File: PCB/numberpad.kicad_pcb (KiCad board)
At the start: 2 copper layers, 97 x 127.2 mm, 73 parts, among them J1 Light_Sensor, J2 Rotary_Encoder, J3 Screen_Connector, J4 FingerPrint_UART, J5 USB_A, J6 Programmer, J7 USB_C_TO_PC, SW0 0, SW1 ., SW10 8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

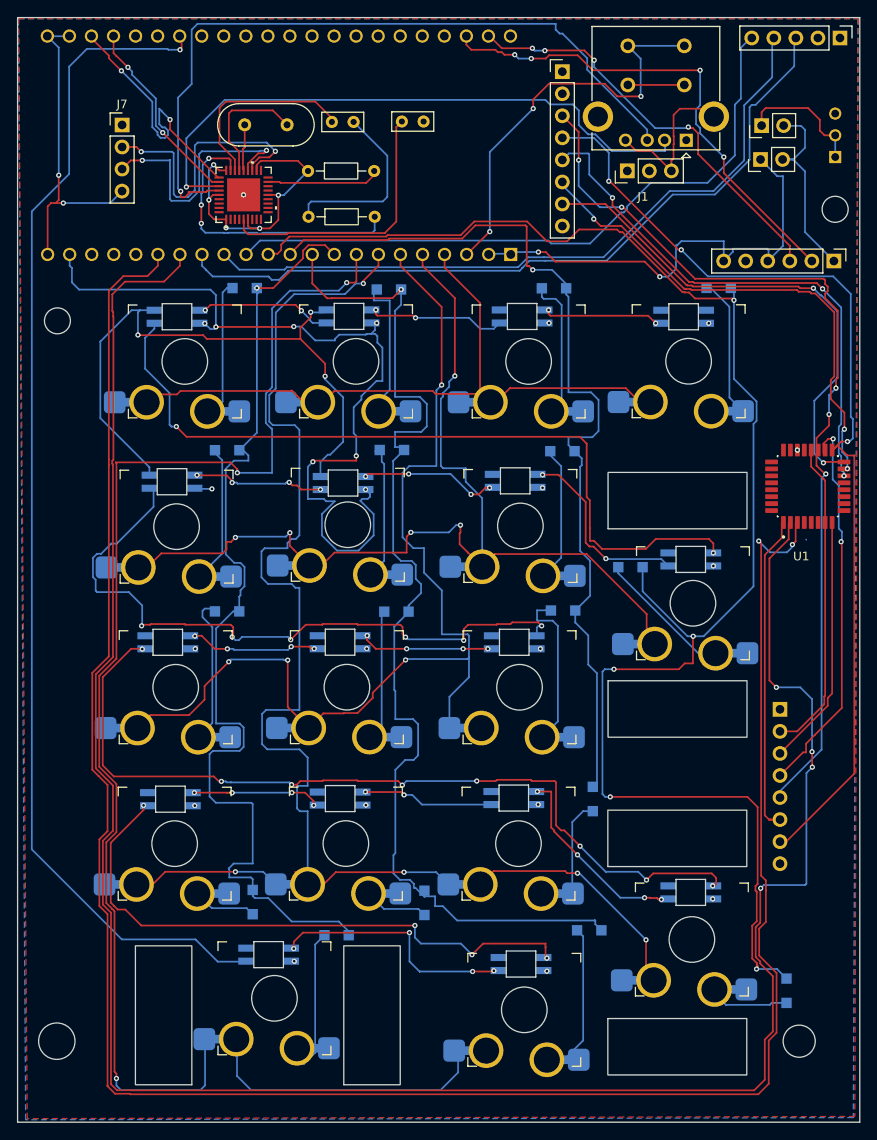
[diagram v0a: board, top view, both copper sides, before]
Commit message: v.1.1
PCB Key spacing, style refresh, web ui bug fix, qol feature implimentation (cart item ajust, remove from cart)
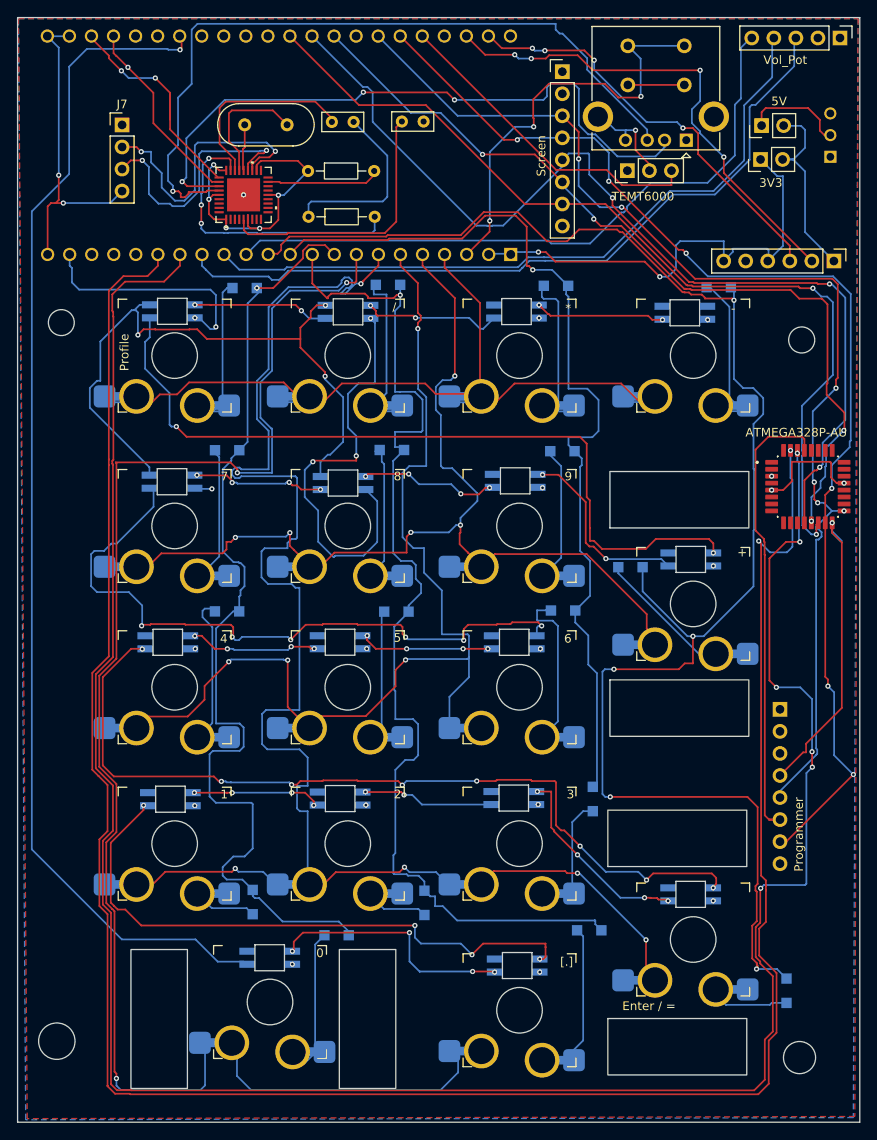
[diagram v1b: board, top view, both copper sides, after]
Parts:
- U1: value ATmega328-P -> ATMEGA328P-AU
- moved SW13 1.35 mm to (58.3, 79.8)
- moved SW15 1.25 mm to (98.0, 79.8)
- moved SW14 1.16 mm to (78.2, 79.8)
- moved D32 0.86 mm to (97.7, 74.7)
- moved SW16 0.84 mm to (118.0, 79.8)
- moved D30 0.83 mm to (58.0, 74.7)
- moved REF** 0.66 mm to (68.5, 154.4)
- moved SW0 0.66 mm to (69.3, 154.2)
- moved S1 0.56 mm to (133.8, 54.4)
- moved SW1 0.55 mm to (98.0, 155.2)
- moved D14 0.55 mm to (82.8, 71.7)
- moved D31 0.54 mm to (78.2, 74.8)
- moved D18 0.48 mm to (97.7, 150.1)
- moved D33 0.48 mm to (117.0, 74.9)
- moved D17 0.38 mm to (69.2, 149.2)
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- renumbered J1 to TEMT6000
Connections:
- S1 pad 1: 5V -> unconnected-(S1-Pad1)
- S1 pad 3: 5V -> unconnected-(S1-Pad3)
- TEMT6000 pad 2: Light_int -> GND
- TEMT6000 pad 3: GND -> Light_int
- U1 pad 1: PC6 -> unconnected-(U1-PD3-Pad1)
- U1 pad 12: unconnected-(U1-PD6-Pad12) -> SCREEN_RST
- U1 pad 13: unconnected-(U1-PD7-Pad13) -> SCREEN_DC
- U1 pad 14: SCREEN_RST -> SCREEN_CS
- U1 pad 15: SCREEN_DC -> PB3
- U1 pad 16: SCREEN_CS -> PB4
- U1 pad 17: PB3 -> PB5
- U1 pad 18: PB4 -> 5V
- U1 pad 19: PB5 -> unconnected-(U1-ADC6-Pad19)
- U1 pad 2: RX -> unconnected-(U1-PD4-Pad2)
- U1 pad 20: 5V -> unconnected-(U1-AREF-Pad20)
- U1 pad 21: unconnected-(U1-AREF-Pad21) -> GND
- U1 pad 22: GND -> unconnected-(U1-ADC7-Pad22)
- U1 pad 29: (no net) -> PC6
- U1 pad 3: TX -> GND
- U1 pad 30: (no net) -> RX
- U1 pad 31: (no net) -> TX
- U1 pad 32: (no net) -> unconnected-(U1-PD2-Pad32)
- U1 pad 4: unconnected-(U1-PD2-Pad4) -> 5V
- U1 pad 5: unconnected-(U1-PD3-Pad5) -> GND
- U1 pad 6: unconnected-(U1-PD4-Pad6) -> 5V
- U1 pad 7: 5V -> unconnected-(U1-PB6-Pad7)
- U1 pad 8: GND -> unconnected-(U1-PB7-Pad8)
- U2 pad J3_10: unconnected-(U2-GPIO38-PadJ3_10) -> SCREEN_RST
- U2 pad J3_11: unconnected-(U2-GPIO37-PadJ3_11) -> SCREEN_CS
- U2 pad J3_5: unconnected-(U2-GPIO2-PadJ3_5) -> Light_int
- U2 pad J3_6: unconnected-(U2-MTMS/GPIO42-PadJ3_6) -> PB3
- U2 pad J3_7: unconnected-(U2-MTDI/GPIO41-PadJ3_7) -> PB5
- U2 pad J3_9: unconnected-(U2-MTCK/GPIO39-PadJ3_9) -> SCREEN_DC
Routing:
- net 5V: track 147.7 -> 90.5 mm, vias 21 -> 19
- net SCREEN_RST: track 61.4 -> 113.2 mm
- net SCREEN_CS: track 58.2 -> 105.9 mm
- net SCREEN_DC: track 56.5 -> 97.1 mm, vias 3 -> 4
- net Light_int: track 0.00 -> 37.5 mm
- net PB5: track 105.9 -> 135.1 mm, vias 5 -> 6
- net PB3: track 114.0 -> 136.2 mm, vias 3 -> 6
- net GND: track 207.8 -> 187.7 mm, vias 7 -> 10
- net PC6: track 37.8 -> 53.5 mm
- net R3: track 181.4 -> 195.2 mm
- net RX: track 255.7 -> 265.2 mm, vias 4 -> 6
- net TX: track 251.2 -> 259.4 mm
- net PB4: track 45.0 -> 37.9 mm, vias 2 -> 1
- net DS-: track 71.0 -> 75.8 mm, vias 1 -> 3
- net R1: track 134.0 -> 129.9 mm
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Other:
- outline, holes or cut-outs redrawn
- board text added: "*"
- board text added: "+"
- board text added: "-"
- board text added: "/"
- board text added: "0"
- board text added: "1"
- board text added: "2"
- board text added: "3"
- board text added: "3V3"
- board text added: "4"
- board text added: "5"
- board text added: "5V"
- board text added: "6"
- board text added: "7"
- board text added: "8"
- board text added: "9"
- board text added: "Enter / ="
- board text added: "Profile"
- board text added: "Programmer"
- board text added: "Reset"
- board text added: "Screen"
- board text added: "Vol_Pot"
- board text added: "[.]"
